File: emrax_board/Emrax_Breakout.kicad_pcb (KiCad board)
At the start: 2 copper layers, 45.7 x 35.6 mm, 4 parts, among them J1 Conn_01x09, J2 Conn_01x09

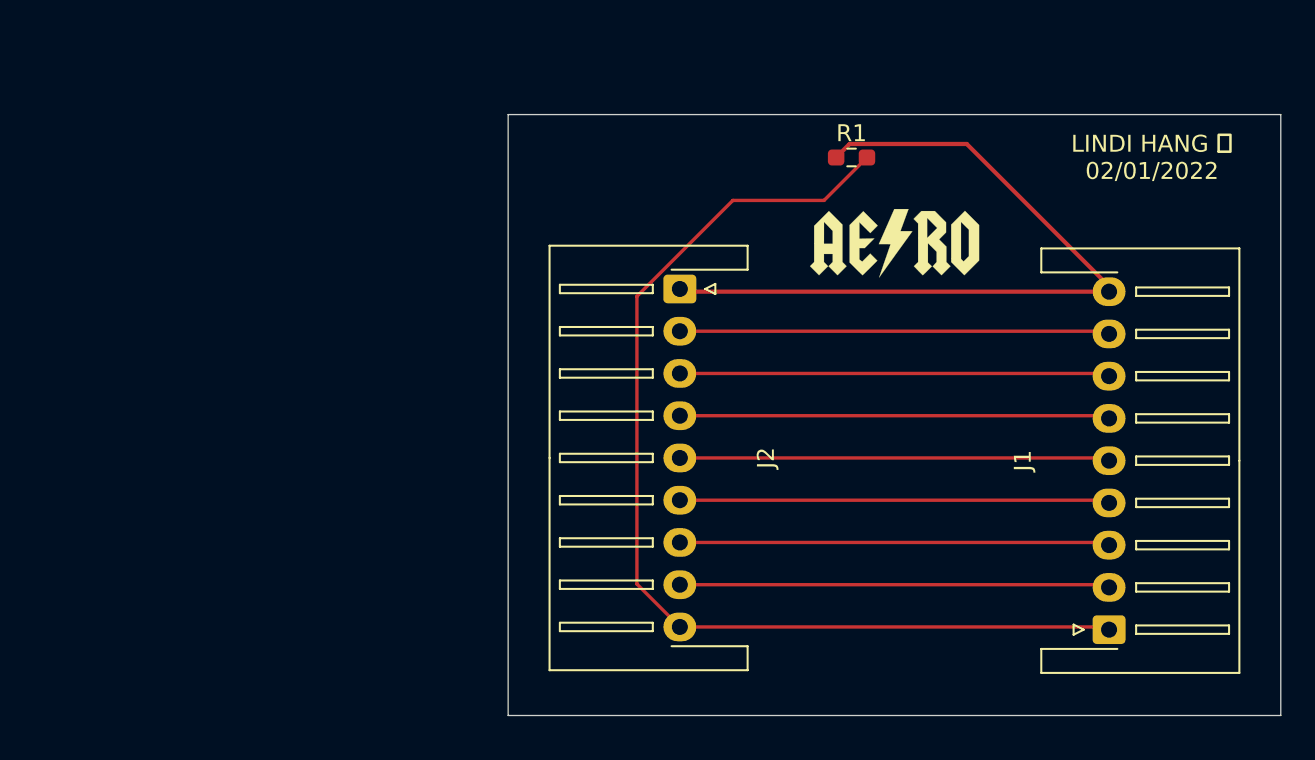
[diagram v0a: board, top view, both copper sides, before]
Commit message: updating emrax breakout board
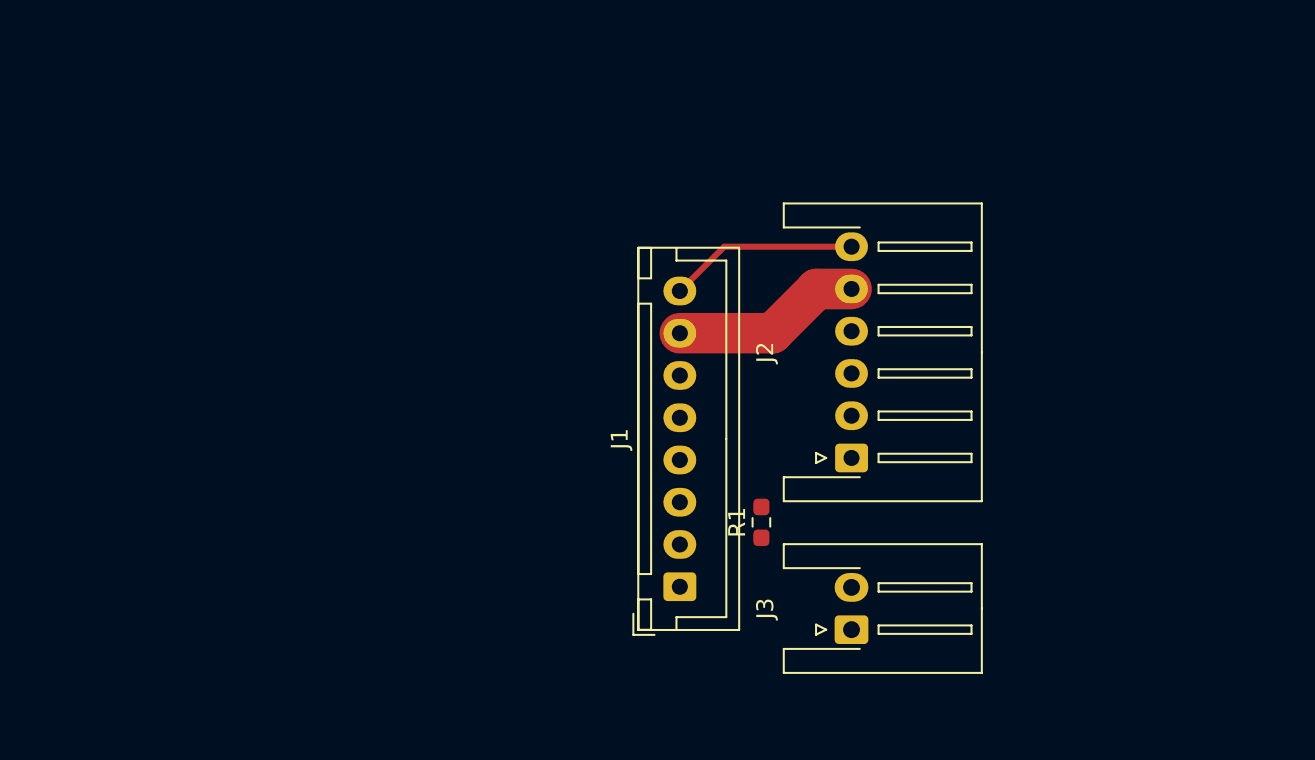
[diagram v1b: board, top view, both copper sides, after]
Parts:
- removed G***: LOGO, AERO_Footprints:AERO_Logo_10x4mm
- added J3: Conn_01x02, Connector_JST:JST_XH_S2B-XH-A-1_1x02_P2.50mm_Horizontal, F.Cu at (144.8, 83.8)
- J1: value Conn_01x09 -> Conn_01x08; footprint Connector_JST:JST_XH_S9B-XH-A-1_1x09_P2.50mm_Horizontal -> Connector_JST:JST_XH_B8B-XH-A_1x08_P2.50mm_Vertical
- J2: value Conn_01x09 -> Conn_01x06; footprint Connector_JST:JST_XH_S9B-XH-A-1_1x09_P2.50mm_Horizontal -> Connector_JST:JST_XH_S6B-XH-A-1_1x06_P2.50mm_Horizontal
- moved J1 25.5 mm to (134.6, 81.3)
- moved R1 22.2 mm to (139.4, 77.5), turned to 90 degrees
- moved J2 14.3 mm to (144.8, 73.7), turned to 90 degrees
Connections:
- J1 pad 1: /TEMP+ -> +5V
- J2 pad 1: /5V -> /SIN+
- J2 pad 2: /ANGLE- -> /SIN-
- J2 pad 3: /ANGLE+ -> /COS+
- J2 pad 5: /COS+ -> /ANGLE+
- J2 pad 6: /SIN- -> /ANGLE-
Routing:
- net /TEMP+: track 63.1 -> 0.00 mm
- net /5V: track 45.4 -> 0.00 mm
- net /TEMP-: track 25.5 -> 0.00 mm
- net /SIN-: track 25.5 -> 0.00 mm
- net /SIN+: track 25.5 -> 0.00 mm
- net /COS-: track 25.5 -> 0.00 mm
- net /COS+: track 25.5 -> 0.00 mm
- net /ANGLE-: track 25.5 -> 11.2 mm
- net /ANGLE+: track 25.4 -> 11.2 mm
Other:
- board outline removed
- board text removed: "LINDI HANG 杭 02/01/2022"

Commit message: change schem and finish layout Ready for Review
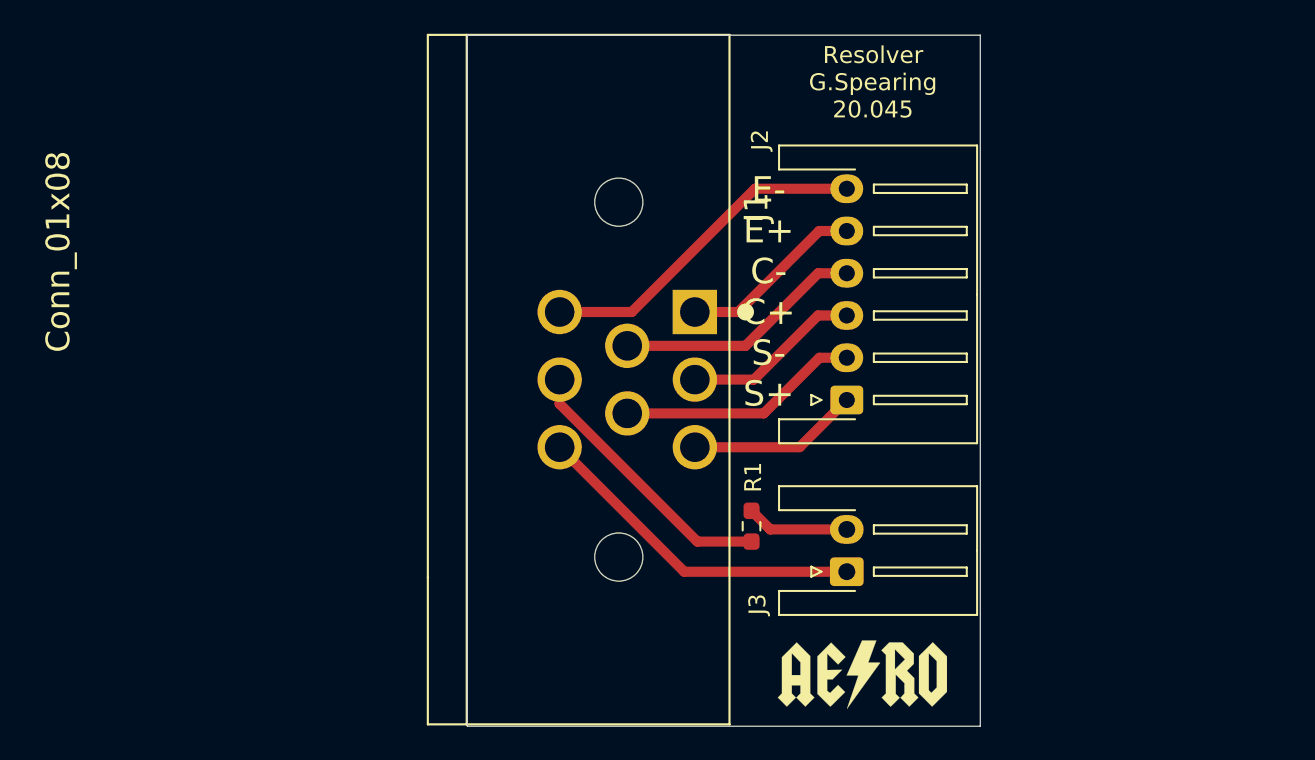
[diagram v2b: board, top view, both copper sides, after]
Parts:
- added G***: LOGO, AERO_Footprints:AERO_Logo_10x4mm, F.Cu at (145.4, 86.5)
- J1: footprint Connector_JST:JST_XH_B8B-XH-A_1x08_P2.50mm_Vertical -> AERO_Footprints:TE_1-776280-1_8pin_Horizontal
- moved J1 12.8 mm to (131.0, 69.0), turned to -90 degrees
- moved J2 3.44 mm to (144.5, 70.2)
- moved J3 3.44 mm to (144.5, 80.4)
- moved R1 0.63 mm to (138.9, 77.7)
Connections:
- J1 pad 1: +5V -> /EXT+
- J1 pad 2: /TEMP- -> /COS+
- J1 pad 4: /SIN- -> /COS-
- J1 pad 5: /COS+ -> /SIN-
- J1 pad 6: /COS- -> /EXT-
- J1 pad 7: /ANGLE+ -> +5V
- J1 pad 8: /ANGLE- -> /TEMP-
- J2 pad 5: /ANGLE+ -> /EXT+
- J2 pad 6: /ANGLE- -> /EXT-
- R1 pad 1: /5V -> +5V
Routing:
- net /TEMP-: track 0.00 -> 20.0 mm
- net /EXT-: track 0.00 -> 20.0 mm
- net +5V: track 0.00 -> 16.2 mm
- net /COS-: track 0.00 -> 14.8 mm
- net /SIN-: track 0.00 -> 14.4 mm
- net /ANGLE-: track 11.2 -> 0.00 mm
- net /ANGLE+: track 11.2 -> 0.00 mm
- net /EXT+: track 0.00 -> 11.0 mm
- net /COS+: track 0.00 -> 10.6 mm
- net /SIN+: track 0.00 -> 10.1 mm
- net /TEMP+: track 0.00 -> 6.10 mm
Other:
- board outline added: 30.4 x 40.9 mm
- board text added: "E- E+ C- C+ S- S+"
- board text added: "Resolver G.Spearing 20.045"

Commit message: touching up layout and making gerbers
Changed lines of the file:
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@@
       (outputformat 1)
       (mirror false)
-      (drillshape 1)
+      (drillshape 0)
       (scaleselection 1)
-      (outputdirectory "")
+      (outputdirectory "Emrax_Gerber/")
     )
   )
@@
     (fp_line (start 3.75 0.6) (end 1.25 0.6) (layer "F.Fab") (width 0.1))
     (fp_line (start 4.95 7.6) (end 4.95 -3.9) (layer "F.Fab") (width 0.1))
-    (pad "1" thru_hole roundrect (at 0 0 90) (size 1.7 2) (drill 1) (layers *.Cu *.Mask) (roundrect_rratio 0.147059)
+    (pad "1" thru_hole roundrect (at 0 0 90) (size 1.7 2) (drill 1) (layers *.Cu *.Mask) (roundrect_rratio 0.1470588235)
       (net 1 "/TEMP-") (pinfunction "Pin_1") (pintype "passive"))
     (pad "2" thru_hole oval (at 2.5 0 90) (size 1.7 2) (drill 1) (layers *.Cu *.Mask)
@@
     (fp_line (start -1.25 0.6) (end 6.25 0.6) (layer "F.Fab") (width 0.1))
     (fp_line (start -0.625 0.6) (end 0 -0.4) (layer "F.Fab") (width 0.1))
-    (pad "1" thru_hole roundrect (at 0 0 90) (size 1.7 1.95) (drill 0.95) (layers *.Cu *.Mask) (roundrect_rratio 0.147059)
+    (pad "1" thru_hole roundrect (at 0 0 90) (size 1.7 1.95) (drill 0.95) (layers *.Cu *.Mask) (roundrect_rratio 0.1470588235)
       (net 6 "/SIN+") (pinfunction "Pin_1") (pintype "passive"))
     (pad "2" thru_hole oval (at 2.5 0 90) (size 1.7 1.95) (drill 0.95) (layers *.Cu *.Mask)
